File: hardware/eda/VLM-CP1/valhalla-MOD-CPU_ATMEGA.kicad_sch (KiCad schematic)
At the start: 22 parts, among them J1 GPIO, J2 ICSP, J3 BUS, K1 RESET, U1 ATmega328P-P, U4 L78L33_TO92, Y1 7.3728 MHz

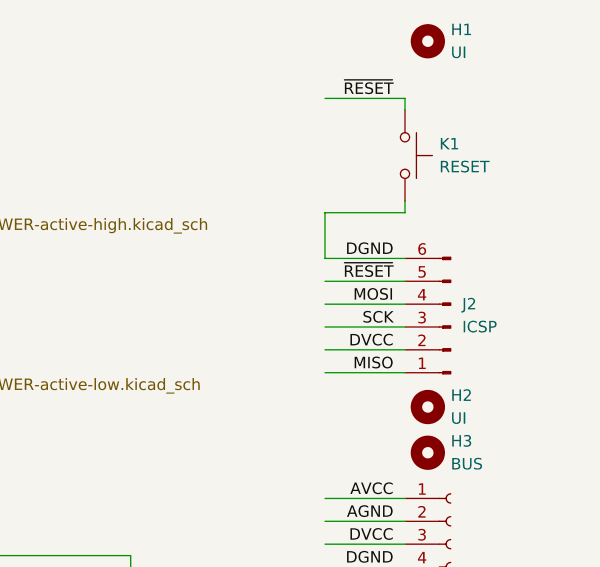
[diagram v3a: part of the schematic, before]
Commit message: UPDATE: progress on component placement for CPU module
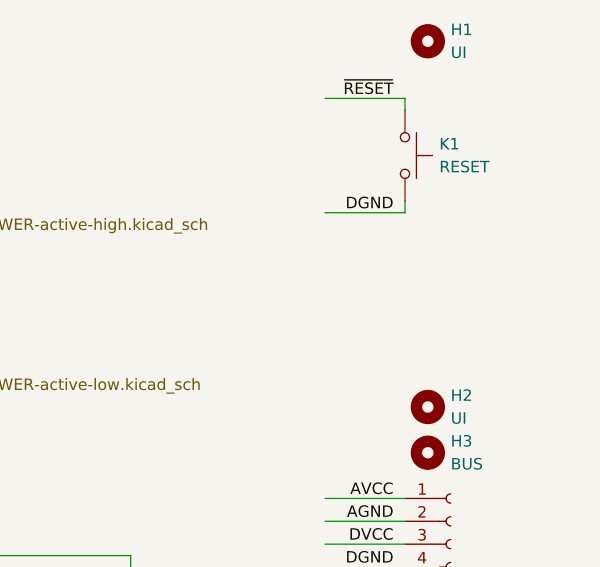
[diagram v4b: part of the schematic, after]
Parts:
- removed J2: ICSP, Connector_IDC:IDC-Header_2x03_P2.54mm_Horizontal, symbol Connector:Conn_01x06_Pin
- C7, C8: footprint (none) -> Capacitor_THT:C_Rect_L4.6mm_W2.0mm_P2.50mm_MKS02_FKP02
- R1, R2: footprint Resistor_THT:R_Axial_DIN0207_L6.3mm_D2.5mm_P10.16mm_Horizontal -> Resistor_THT:R_Axial_DIN0207_L6.3mm_D2.5mm_P5.08mm_Vertical
- Y1: footprint Crystal:Crystal_HC49-U_Horizontal -> Crystal:Crystal_HC49-4H_Vertical
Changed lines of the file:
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@@
 	(wire
 		(pts
-			(xy 261.62 41.91) (xy 270.51 41.91)
-		)
-		(stroke
-			(width 0)
-			(type default)
-		)
-	)
-	(wire
-		(pts
 			(xy 146.05 95.25) (xy 154.94 95.25)
 		)
@@
 	(wire
 		(pts
-			(xy 261.62 46.99) (xy 270.51 46.99)
-		)
-		(stroke
-			(width 0)
-			(type default)
-		)
-	)
-	(wire
-		(pts
 			(xy 69.85 60.96) (xy 80.01 60.96)
 		)
@@
 	(wire
 		(pts
-			(xy 261.62 52.07) (xy 270.51 52.07)
-		)
-		(stroke
-			(width 0)
-			(type default)
-		)
-	)
-	(wire
-		(pts
 			(xy 146.05 78.74) (xy 146.05 77.47)
 		)
@@
 	(wire
 		(pts
-			(xy 261.62 49.53) (xy 270.51 49.53)
-		)
-		(stroke
-			(width 0)
-			(type default)
-		)
-	)
-	(wire
-		(pts
 			(xy 127 67.31) (xy 135.89 67.31)
 		)
@@
 	(wire
 		(pts
-			(xy 261.62 36.83) (xy 261.62 41.91)
-		)
-		(stroke
-			(width 0)
-			(type default)
-		)
-	)
-	(wire
-		(pts
 			(xy 261.62 91.44) (xy 270.51 91.44)
 		)
@@
 	(wire
 		(pts
-			(xy 261.62 44.45) (xy 270.51 44.45)
-		)
-		(stroke
-			(width 0)
-			(type default)
-		)
-	)
-	(wire
-		(pts
 			(xy 34.29 21.59) (xy 57.15 21.59)
 		)
@@
 	(wire
 		(pts
-			(xy 261.62 54.61) (xy 270.51 54.61)
-		)
-		(stroke
-			(width 0)
-			(type default)
-		)
-	)
-	(wire
-		(pts
 			(xy 69.85 78.74) (xy 80.01 78.74)
 		)
@@
 		)
 	)
-	(label "MOSI"
-		(at 269.24 46.99 180)
-		(effects
-			(font
-				(size 1.27 1.27)
-			)
-			(justify right bottom)
-		)
-	)
 	(label "GPIO7"
 		(at 27.94 182.88 90)
@@
 		)
 	)
-	(label "SCK"
-		(at 269.24 49.53 180)
-		(effects
-			(font
-				(size 1.27 1.27)
-			)
-			(justify right bottom)
-		)
-	)
 	(label "~{IINT}"
 		(at 134.62 85.09 180)
@@
 		)
 	)
-	(label "MISO"
-		(at 269.24 54.61 180)
-		(effects
-			(font
-				(size 1.27 1.27)
-			)
-			(justify right bottom)
-		)
-	)
 	(label "SDA"
 		(at 269.24 99.06 180)
@@
 	)
 	(label "DGND"
-		(at 269.24 41.91 180)
+		(at 269.24 36.83 180)
 		(effects
 			(font
@@
 		)
 	)
-	(label "~{RESET}"
-		(at 269.24 44.45 180)
-		(effects
-			(font
-				(size 1.27 1.27)
-			)
-			(justify right bottom)
-		)
-	)
 	(label "DGND"
 		(at 46.99 102.87 0)
@@
 		)
 	)
-	(label "DVCC"
-		(at 269.24 52.07 180)
-		(effects
-			(font
-				(size 1.27 1.27)
-			)
-			(justify right bottom)
-		)
-	)
 	(label "GPIO4"
 		(at 35.56 182.88 90)
@@
 			)
 		)
-		(property "Footprint" "Resistor_THT:R_Axial_DIN0207_L6.3mm_D2.5mm_P10.16mm_Horizontal"
+		(property "Footprint" "Resistor_THT:R_Axial_DIN0207_L6.3mm_D2.5mm_P5.08mm_Vertical"
 			(at 108.712 60.96 90)
 			(effects
@@
 			)
 		)
-		(property "Footprint" ""
+		(property "Footprint" "Capacitor_THT:C_Rect_L4.6mm_W2.0mm_P2.50mm_MKS02_FKP02"
 			(at 240.9952 100.33 0)
 			(effects
@@
 	)
 	(symbol
-		(lib_id "Connector:Conn_01x06_Pin")
-		(at 275.59 49.53 180)
-		(unit 1)
-		(exclude_from_sim no)
-		(in_bom yes)
-		(on_board yes)
-		(dnp no)
-		(fields_autoplaced yes)
-		(property "Reference" "J2"
-			(at 276.86 46.9899 0)
-			(effects
-				(font
-					(size 1.27 1.27)
-				)
-				(justify right)
-			)
-		)
-		(property "Value" "ICSP"
-			(at 276.86 49.5299 0)
-			(effects
-				(font
-					(size 1.27 1.27)
-				)
-				(justify right)
-			)
-		)
-		(property "Footprint" "Connector_IDC:IDC-Header_2x03_P2.54mm_Horizontal"
-			(at 275.59 49.53 0)
-			(effects
-				(font
-					(size 1.27 1.27)
-				)
-				(hide yes)
-			)
-		)
-		(property "Datasheet" "~"
-			(at 275.59 49.53 0)
-			(effects
-				(font
-					(size 1.27 1.27)
-				)
-				(hide yes)
-			)
-		)
-		(property "Description" "Generic connector, single row, 01x06, script generated"
-			(at 275.59 49.53 0)
-			(effects
-				(font
-					(size 1.27 1.27)
-				)
-				(hide yes)
-			)
-		)
-		(pin "2"
-		)
-		(pin "3"
-		)
-		(pin "6"
-		)
-		(pin "1"
-		)
-		(pin "4"
-		)
-		(pin "5"
-		)
-		(instances
-			(project ""
-				(path "/f06f94c1-3b85-417f-a10f-1ec163aec97d"
-					(reference "J2")
-					(unit 1)
-				)
-			)
-		)
-	)
-	(symbol
 		(lib_id "Switch:SW_Push")
 		(at 270.51 30.48 270)
@@
 			)
 		)
-		(property "Footprint" ""
+		(property "Footprint" "Capacitor_THT:C_Rect_L4.6mm_W2.0mm_P2.50mm_MKS02_FKP02"
 			(at 219.4052 100.33 0)
 			(effects
@@
 			)
 		)
-		(property "Footprint" "Resistor_THT:R_Axial_DIN0207_L6.3mm_D2.5mm_P10.16mm_Horizontal"
+		(property "Footprint" "Resistor_THT:R_Axial_DIN0207_L6.3mm_D2.5mm_P5.08mm_Vertical"
 			(at 116.332 60.96 90)
 			(effects
@@
 			)
 		)
-		(property "Footprint" "Crystal:Crystal_HC49-U_Horizontal"
+		(property "Footprint" "Crystal:Crystal_HC49-4H_Vertical"
 			(at 87.63 49.53 0)
 			(effects

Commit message: UPDATE: progress towards templatizing dimensions   - used the PSU module as a master copy for now until the template     stabilizes, to be exported as a stand-alone blueprint for future     modules   - minor progress on the CPU(ATMega) module: easier to solder     footprint for LVCC regulator, crystal dress-up and reference     clean-ups.
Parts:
- U4: footprint Package_TO_SOT_THT:TO-92_Inline -> Package_TO_SOT_THT:TO-92_Wide
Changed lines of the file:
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@@
 			)
 		)
-		(property "Footprint" "Package_TO_SOT_THT:TO-92_Inline"
+		(property "Footprint" "Package_TO_SOT_THT:TO-92_Wide"
 			(at 231.14 81.915 0)
 			(effects

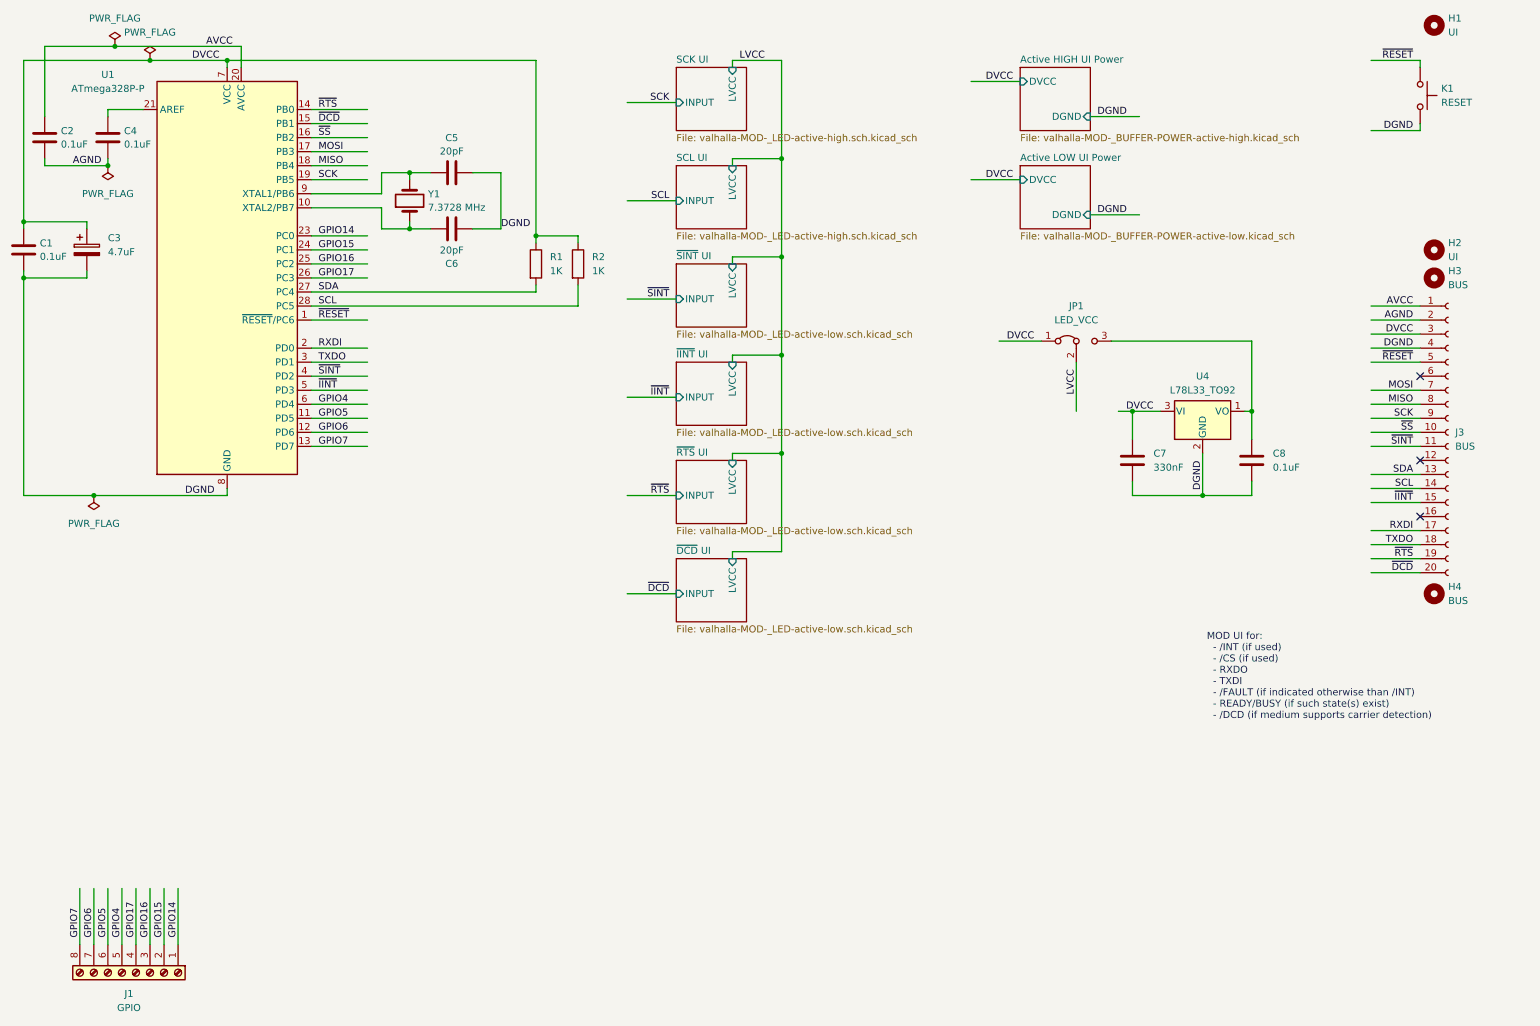
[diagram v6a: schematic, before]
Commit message: UPDATE: PSU and CPU(ATMega-T) artwork complete
 - also extracted the existing PSU as a template for future modules
 - PSU final touches and RTM
 - CPU(ATMega-T) tied unused inputs to GND, fixed all DRC violations,
   dressed-up silkscreen and RTM.
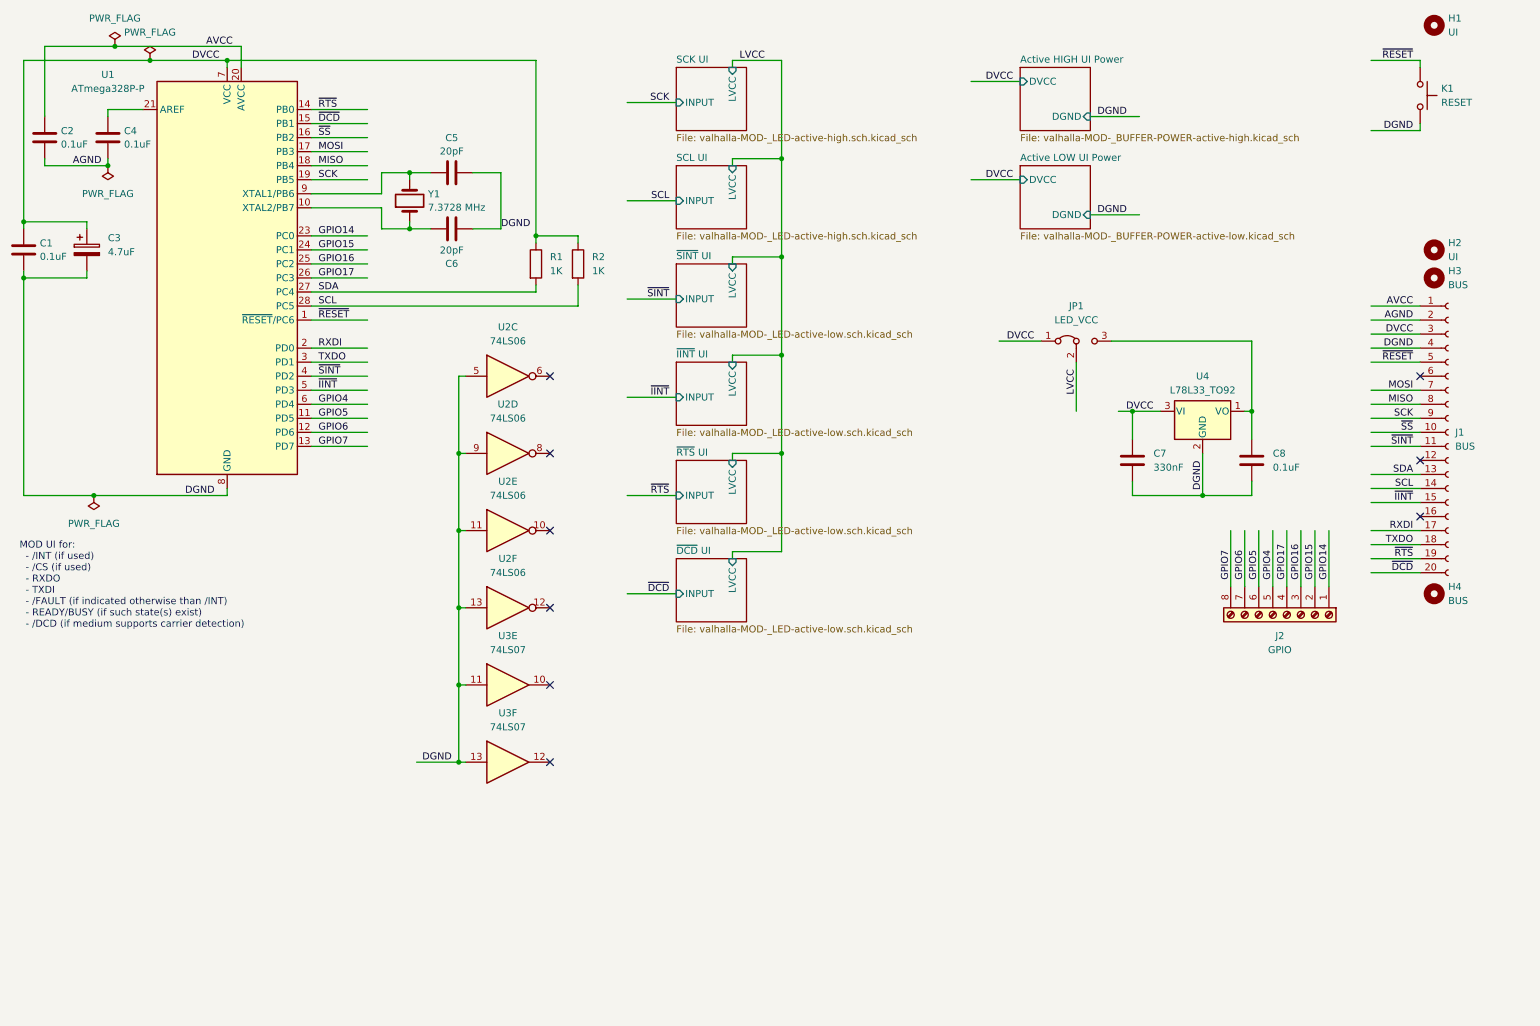
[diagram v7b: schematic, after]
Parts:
- added U2: 74LS06, symbol 74xx:74LS06
- added U3: 74LS07, symbol 74xx:74LS07
- renumbered J3 to J1, J1 to J2
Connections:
- net DGND: now also U2.11, U2.13, U2.5, U2.9, U3.11, U3.13
- no-connect marks 3 -> 9
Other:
- moved on the sheet: J2

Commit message: UPDATE: updated MOD-CPU(ATMega) to match the latest specification.
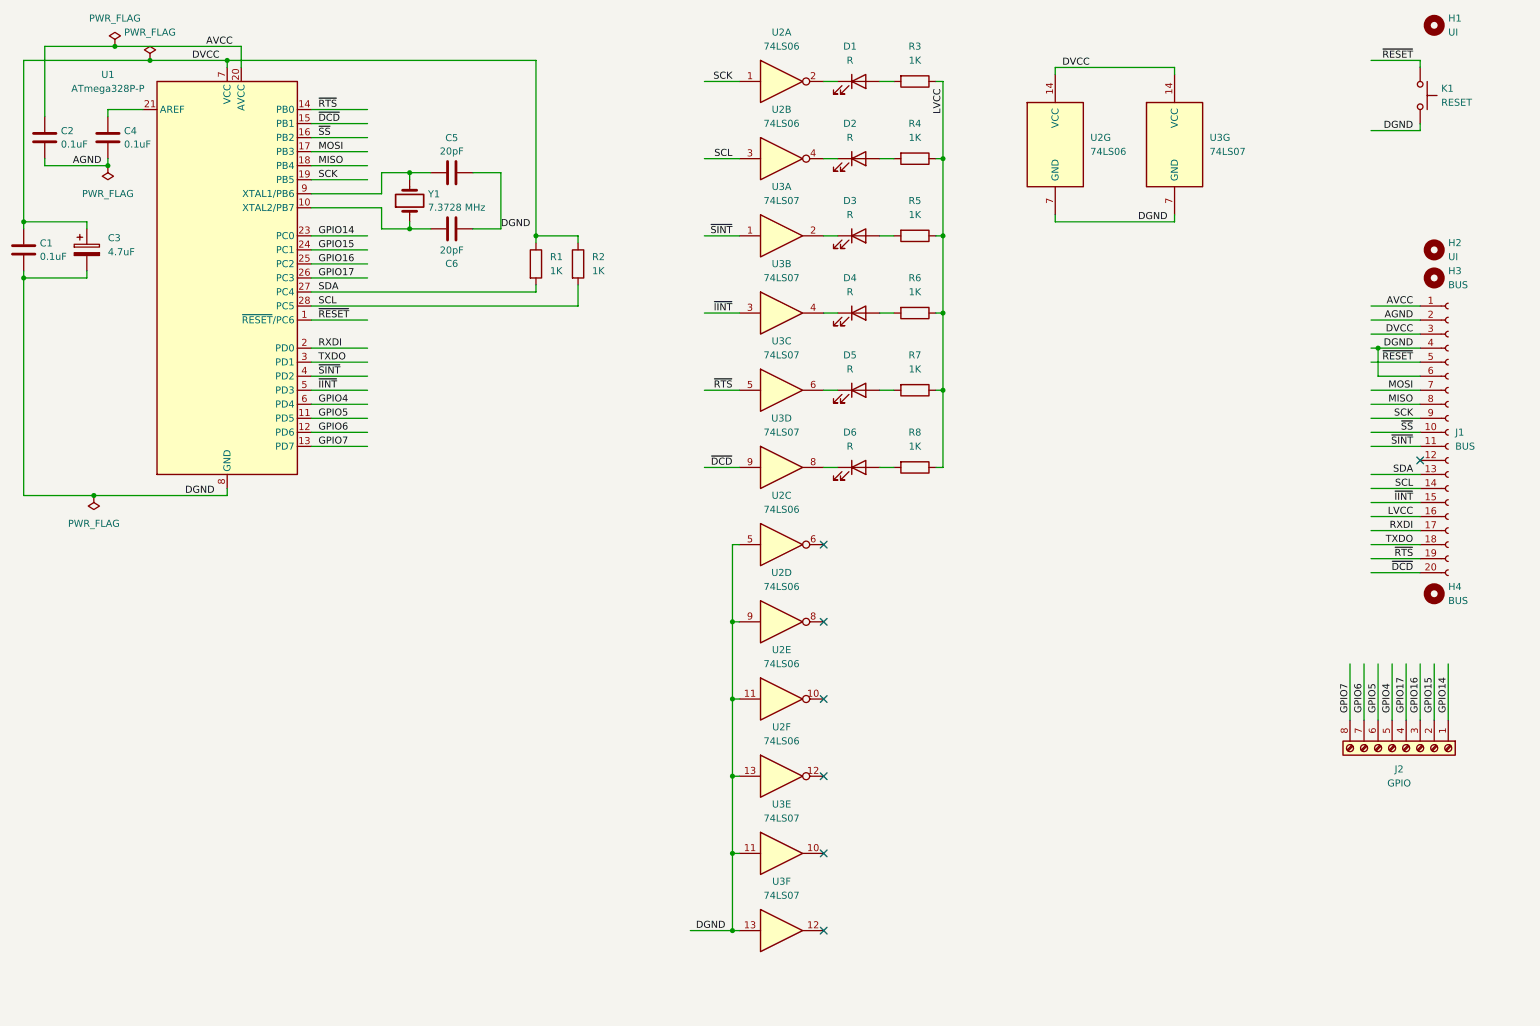
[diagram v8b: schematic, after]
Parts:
- removed C7: 330nF, Capacitor_THT:C_Rect_L4.6mm_W2.0mm_P2.50mm_MKS02_FKP02, symbol Device:C
- removed C8: 0.1uF, Capacitor_THT:C_Rect_L4.6mm_W2.0mm_P2.50mm_MKS02_FKP02, symbol Device:C
- removed JP1: LED_VCC, Connector_PinHeader_2.54mm:PinHeader_1x03_P2.54mm_Vertical, symbol Jumper:Jumper_3_Bridged12
- removed U4: L78L33_TO92, Package_TO_SOT_THT:TO-92_Wide, symbol Regulator_Linear:L78L33_TO92
- added D1, D2, D3, D4, D5, D6: R, LED_THT:LED_D3.0mm_Horizontal_O1.27mm_Z2.0mm, symbol Device:LED
- added R3, R4, R5, R6, R7, R8: 1K, Resistor_THT:R_Axial_DIN0207_L6.3mm_D2.5mm_P5.08mm_Vertical, symbol Device:R
- added unit 1 of U2
- added unit 7 of U2
- added unit 3 of U2
- added unit 7 of U3
- added unit 4 of U3
- added unit 3 of U3
- added unit 2 of U3
- added unit 5 of U3
- U2, U3: footprint (none) -> Package_DIP:DIP-14_W7.62mm
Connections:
- net DGND: now also J1.6 (Pin_6), U2.5, U2.7 (GND), U3.11, U3.7 (GND); no longer U2.5, U3.11
- net DVCC: now also U2.14 (VCC), U3.14 (VCC)
- net LVCC: now also J1.16 (Pin_16), R3.1, R4.1, R5.1, R6.1, R7.1, R8.1
- net SCK: now also U2.1
- net SCL: now also U2.3
- net ~{DCD}: now also U3.9
- net ~{IINT}: now also U3.3
- net ~{RTS}: now also U3.5
- net ~{SINT}: now also U3.1
- new net: D3.1 (K), U3.2
- new net: D3.2 (A), R5.2
- new net: D2.1 (K), U2.4
- new net: D1.1 (K), U2.2
- new net: D2.2 (A), R4.2
- new net: D6.1 (K), U3.8
- new net: D5.1 (K), U3.6
- new net: D4.1 (K), U3.4
- new net: D1.2 (A), R3.2
- new net: D4.2 (A), R6.2
- new net: D6.2 (A), R8.2
- new net: D5.2 (A), R7.2
- no-connect marks 9 -> 7
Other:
- removed sheet Active HIGH UI Power
- removed sheet Active LOW UI Power
- removed sheet SCK UI
- removed sheet SCL UI
- removed sheet ~{DCD} UI
- removed sheet ~{IINT} UI
- removed sheet ~{RTS} UI
- removed sheet ~{SINT} UI
- note removed: "MOD UI for: - /INT (if used) - /CS (if used) - RXDO - TXDI - /FAULT (if indicated otherwise than /INT) - READY/BUSY (if such state(s) exist) - /DCD (if medium supports carrier detection)"
- title: (none) -> Valhalla MOD-CPU(ATMega)
- moved on the sheet: J2, U2B, U2D, U2E, U2F, U3A, U3F
